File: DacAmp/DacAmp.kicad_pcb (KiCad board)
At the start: 4 copper layers, 110.5 x 101.6 mm, 114 parts, among them J1 AudioPlug3, J2 USB_B, U1 PCM2906C, U10 TLV70237_SOT23-5, U11 TLV61046ADB, U12 NE5532, U13 LM2941LD_NOPB, U2 NE5532, U3 NE5532, U4 NE5532, U5 NE5532, U6 NE5532, U7 NE5532, U8 NE5532, U9 NE5532, Y1 12MHz

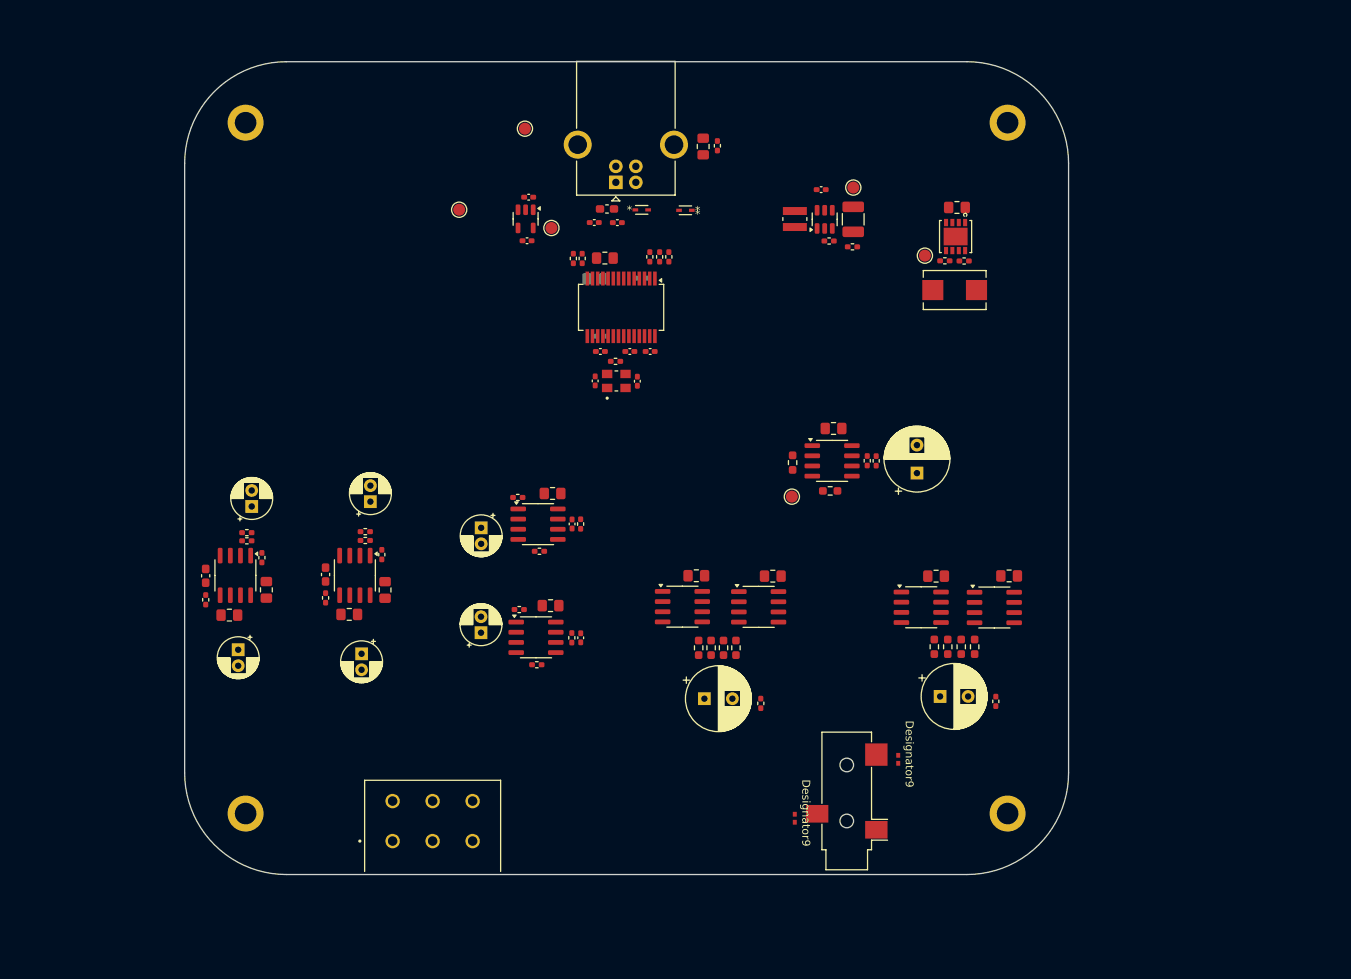
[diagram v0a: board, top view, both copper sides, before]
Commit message: do way too much routing in one commit
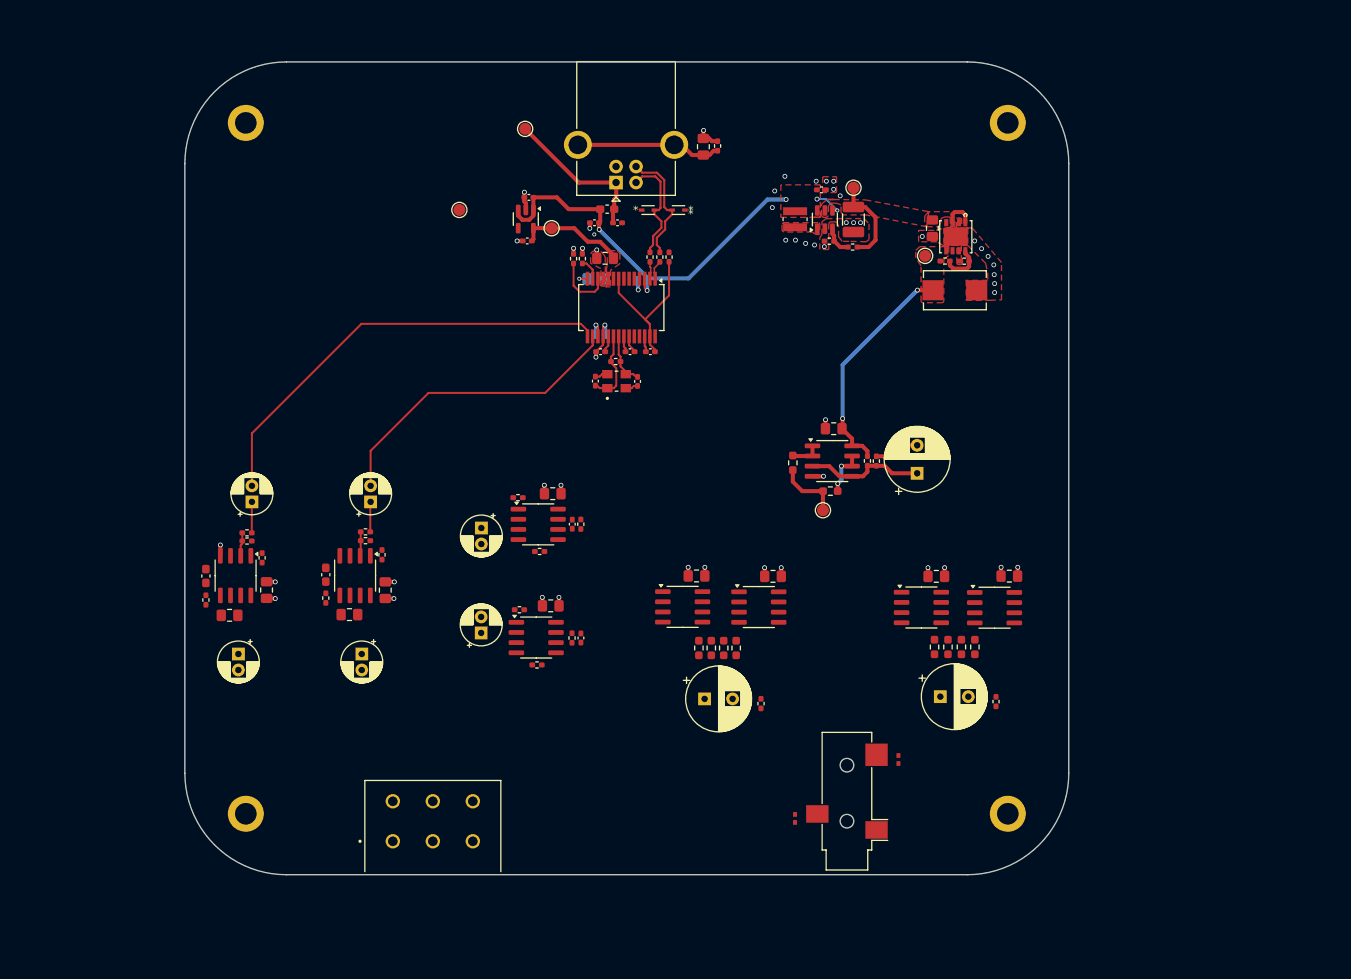
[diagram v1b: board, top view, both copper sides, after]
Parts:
- moved TP3 4.24 mm to (112.4, 81.2)
- moved C38 4.02 mm to (126.1, 46.0), turned to -90 degrees
- moved D2 0.86 mm to (94.4, 43.7)
- moved D1 0.79 mm to (90.6, 43.7)
- moved C11 0.58 mm to (41.0, 80.2)
- moved C19 0.53 mm to (39.4, 99.2)
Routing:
- net /Codec/VOUTR: track 0.00 -> 55.3 mm
- net VBUS: track 0.00 -> 53.8 mm, vias 0 -> 5
- net GND: track 0.00 -> 42.0 mm, vias 0 -> 46
- net /Codec/VOUTL: track 0.00 -> 38.7 mm
- net 15V: track 0.00 -> 37.4 mm, vias 0 -> 10
- net VDDI: track 0.00 -> 20.3 mm
- net VUSB_CONN: track 0.00 -> 19.4 mm
- net CGND: track 0.00 -> 18.2 mm
- net 17V: track 0.00 -> 15.1 mm
- net /Power/7V5_IN: track 0.00 -> 15.0 mm
- net /Codec/CONN_D+: track 0.00 -> 15.0 mm
- net /Codec/CONN_D-: track 0.00 -> 14.0 mm
- net 3V7: track 0.00 -> 13.5 mm
- net /Codec/XTO: track 0.00 -> 9.44 mm
- net 7V5: track 0.00 -> 8.12 mm
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- added copper zone on F.Cu, net /Power/SW
- added copper zone on F.Cu, net 15V
- added copper zone on F.Cu, net 17V
- added copper zone on F.Cu, net 3V7
- added copper zone on F.Cu, net GND
- added copper zone on F.Cu, net VBUS

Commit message: complete layout
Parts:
- U13: footprint LM2941:DFN400X400X80-9N -> LM2941:NGN0008A
- moved C12 1.14 mm to (69.7, 97.7), turned to -90 degrees
- moved C20 0.51 mm to (54.3, 99.2)
- moved R22 0.13 mm to (40.3, 84.1)
- moved R40 0.13 mm to (40.3, 85.1)
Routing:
- net 15V: track 37.4 -> 194.6 mm
- net 7V5: track 8.12 -> 147.7 mm, vias 0 -> 9
- net /Output stage/PREAMP_OUT_L: track 0.00 -> 106.6 mm, vias 0 -> 2
- net /Output stage/PREAMP_OUT_R: track 0.00 -> 63.5 mm
- net /Preamp/Dual-Gang Potentiometer/POT_WIPER_L: track 0.00 -> 35.8 mm
- net /Preamp/Dual-Gang Potentiometer/FILT_OUT_R: track 0.00 -> 32.4 mm
- net /Preamp/Dual-Gang Potentiometer/POT_WIPER_R: track 0.00 -> 25.4 mm
- net /Output stage/STEREO_OUT_R: track 0.00 -> 23.9 mm
- net GND: track 42.0 -> 61.5 mm, vias 46 -> 709
- net /Preamp/Dual-Gang Potentiometer/FILT_OUT_L: track 0.00 -> 18.2 mm
- net /Output stage/STEREO_OUT_L: track 0.00 -> 18.0 mm
- net Net-(C17-Pad1): track 0.00 -> 14.5 mm, vias 0 -> 2
- net Net-(C23-Pad1): track 0.00 -> 13.9 mm, vias 0 -> 2
- net /Output stage/BUF4_OUT_R: track 0.00 -> 13.7 mm
- net /Output stage/BUF4_OUT_L: track 0.00 -> 12.3 mm
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- added copper zone on F.Cu, net /Output stage/BUFS_OUT_L
- added copper zone on F.Cu, net /Output stage/BUFS_OUT_R
- added copper zone on B.Cu, net GND
- added copper zone on F.Cu, net VDDI
